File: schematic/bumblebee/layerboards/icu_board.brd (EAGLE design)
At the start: 85 x 100 mm, 20 parts, among them P1 B5B-EH-A

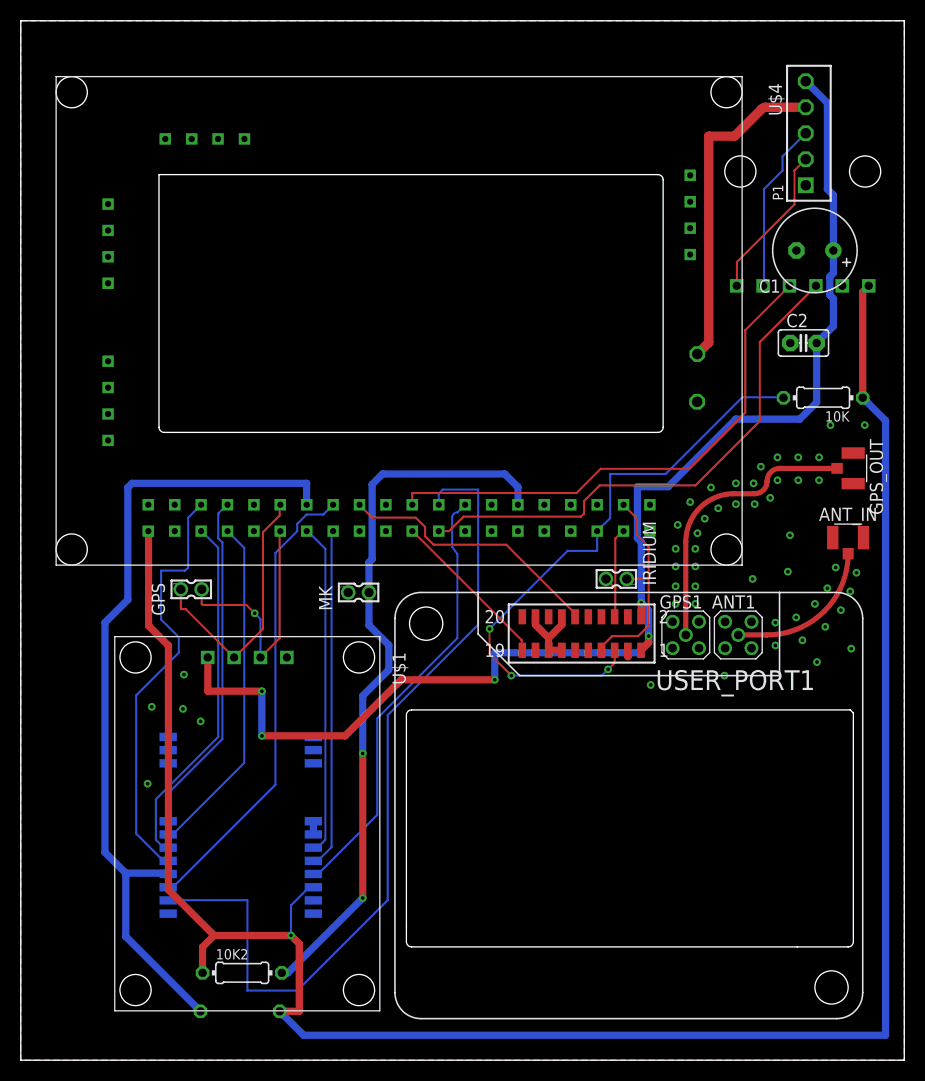
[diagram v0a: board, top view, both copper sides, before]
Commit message: CCU и ICU полностью готовы. Было бы здорово, если бы ещё кто-то посмотрел По SCU требуются уточнения
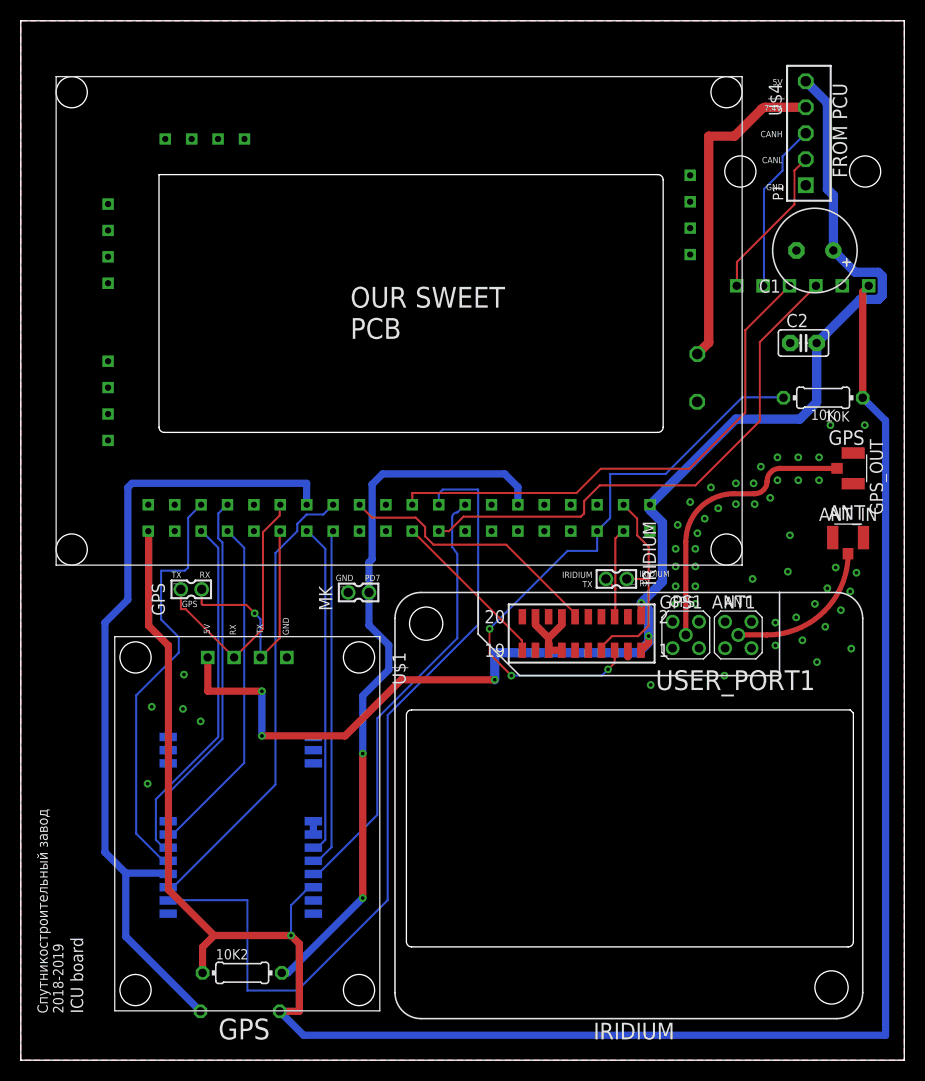
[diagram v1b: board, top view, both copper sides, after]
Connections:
- net 5V_ICU: now also U$4.5V_0
- net GND: now also U$4.GND_0, U$4.GND_1
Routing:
- net 5V_ICU: track 127.2 -> 132.1 mm
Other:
- outline, holes or cut-outs redrawn
- board text added: "10K"
- board text added: "3V3"
- board text added: "5V"
- board text added: "7.4V"
- board text added: "AMPLIFIER"
- board text added: "ANT"
- board text added: "CAN"
- board text added: "CANH"
- board text added: "CANL"
- board text added: "CRX"
- board text added: "CTX"
- board text added: "FROM PCU"
- board text added: "GND"
- board text added: "GPS"
- board text added: "ICU board"
- board text added: "IRIDIUM"
- board text added: "IRIDIUM RX"
- board text added: "IRIDIUM TX"
- board text added: "OUR SWEET PCB"
- board text added: "PD7"
- board text added: "RF"
- board text added: "RX"
- board text added: "TX"
- board text added: "Спутникостроительный завод 2018-2019"
- board text added: "Спутникостроительный завод имени композитора Юрия Шостаковича 2018-2019"

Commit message: ICU готова, SCU скоро доделаю, пока что там всё не очень В либу добавлен LSM303C
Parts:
- added DEBUG: 332-02, con-garry:332-02
- added P2: B8B-EH-A, con-jst-eh:B8B-EH-A
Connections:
- removed net N$11: 10K2.2, MK.2, U$4.PD7
- removed net PD8=TX: GPS.1, U$1.RX, U$4.PD8
- removed net PD9=RX: GPS.2, U$1.TX, U$4.PD9
- new net PD7: 10K2.2, MK.2, P2.8, U$4.PD7
- new net RX_GPS: GPS.1, P2.6, U$1.RX
- new net SWC: DEBUG.2, P2.2
- new net SWD: DEBUG.1, P2.1
- new net TX_GPS: GPS.2, P2.5, U$1.TX, U$4.PD9
- net DF_S_RX: now also P2.4
- net DF_S_TX: now also P2.3
- net GND: now also P2.7
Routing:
- net SWC: track 0.00 -> 117.2 mm
- net SWD: track 0.00 -> 111.1 mm
- net PD7: track 0.00 -> 102.2 mm, vias 0 -> 2
- net DF_S_TX: track 9.93 -> 86.5 mm, vias 0 -> 1
- net DF_S_RX: track 20.4 -> 96.1 mm
- net N$11: track 69.2 -> 0.00 mm, vias 2 -> 0
- net TX_GPS: track 0.00 -> 46.6 mm, vias 0 -> 3
- net RX_GPS: track 0.00 -> 27.5 mm, vias 0 -> 2
- net PD8=TX: track 25.5 -> 0.00 mm
- net PD9=RX: track 24.3 -> 0.00 mm, vias 1 -> 0
- net N$16: track 41.1 -> 39.1 mm
- net ON_OFF: track 58.1 -> 56.1 mm
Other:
- board text added: "DEBUG"
- board text added: "Test Mode"
- board text removed: "AMPLIFIER"
- board text removed: "OUR SWEET PCB"
- board text removed: "Спутникостроительный завод имени композитора Юрия Шостаковича 2018-2019"

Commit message: Подготовка плат к производству
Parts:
- renumbered GPS to GPS_DBG, JP1 to V7.4, JP2 to GND, MK to TEST_MODE, P1 to FROM_PCU, P2 to DEBUG_OUT, U$1 to GPS_BRD, U$3 to RF, U$4 to GREENBRD, U$5 to CAN
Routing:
- net GND: track 12.3 -> 8.86 mm, vias 47 -> 45
- net 5V_ICU: track 132.1 -> 134.7 mm
- net SWC: track 117.2 -> 118.7 mm
- net DF_S_RX: track 96.1 -> 97.3 mm
- net DF_RI: track 25.9 -> 26.7 mm
- net N$16: track 39.1 -> 39.7 mm
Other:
- board text removed: "CAN"
- board text removed: "DEBUG"
- board text removed: "FROM PCU"
- board text removed: "IRIDIUM"
- board text removed: "RF"
- board text removed: "Test Mode"
